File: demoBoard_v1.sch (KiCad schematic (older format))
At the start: 55 parts, among them P1 SPI_Header, P10 RTC_Serial, P11 WD_Header, P12 WD_1.2V_NC, P13 RTC_Aux, P14 Flash_3v3_NC, P15 WD_SENSE_3.3V_NC, P2 3x_CS_Header, P3 Power_Header, P4 LOAD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

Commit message: Updated footprints for headers in schematic
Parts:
- P1, P13, P2, P6, P7: footprint SFUSat:3x_01In_Header -> SFUSat:3x_01In_Header_v2
- P10: footprint SFUSat:4x01In_Header -> SFUSat:4x01In_Header_v2
- P11, P12, P14, P15, P3, P4, P5, P8, P9: footprint SFUSat:2x01In_Header -> SFUSat:2x01In_Header_v2
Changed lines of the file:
@@
 F 0 "P1" H 1750 2600 50  0000 C CNN
 F 1 "SPI_Header" V 1850 2400 50  0000 C CNN
-F 2 "SFUSat:3x_01In_Header" H 1750 2400 50  0001 C CNN
+F 2 "SFUSat:3x_01In_Header_v2" H 1750 2400 50  0001 C CNN
 F 3 "" H 1750 2400 50  0000 C CNN
 	1    1750 2400
@@
 F 0 "P2" H 2950 2650 50  0000 C CNN
 F 1 "3x_CS_Header" V 3050 2450 50  0000 C CNN
-F 2 "SFUSat:3x_01In_Header" H 2950 2450 50  0001 C CNN
+F 2 "SFUSat:3x_01In_Header_v2" H 2950 2450 50  0001 C CNN
 F 3 "" H 2950 2450 50  0000 C CNN
 	1    2950 2450
@@
 F 0 "P3" H 5000 6900 50  0000 C CNN
 F 1 "Power_Header" V 5100 6750 50  0000 C CNN
-F 2 "SFUSat:2x01In_Header" H 5000 6750 50  0001 C CNN
+F 2 "SFUSat:2x01In_Header_v2" H 5000 6750 50  0001 C CNN
 F 3 "" H 5000 6750 50  0000 C CNN
 	1    5000 6750
@@
 F 0 "P10" H 8100 6400 50  0000 C CNN
 F 1 "RTC_Serial" V 8200 6150 50  0000 C CNN
-F 2 "SFUSat:4x01In_Header" H 8100 6150 50  0001 C CNN
+F 2 "SFUSat:4x01In_Header_v2" H 8100 6150 50  0001 C CNN
 F 3 "" H 8100 6150 50  0000 C CNN
 	1    8100 6150
@@
 F 0 "P13" H 10050 6350 50  0000 C CNN
 F 1 "RTC_Aux" V 10150 6150 50  0000 C CNN
-F 2 "SFUSat:3x_01In_Header" H 10050 6150 50  0001 C CNN
+F 2 "SFUSat:3x_01In_Header_v2" H 10050 6150 50  0001 C CNN
 F 3 "" H 10050 6150 50  0000 C CNN
 	1    10050 6150
@@
 F 0 "P7" H 3950 4150 50  0000 C CNN
 F 1 "INA_Power" V 4050 3950 50  0000 C CNN
-F 2 "SFUSat:3x_01In_Header" H 3950 3950 50  0001 C CNN
+F 2 "SFUSat:3x_01In_Header_v2" H 3950 3950 50  0001 C CNN
 F 3 "" H 3950 3950 50  0000 C CNN
 	1    3950 3950
@@
 F 0 "P6" H 2350 3400 50  0000 C CNN
 F 1 "INA_GND" V 2450 3200 50  0000 C CNN
-F 2 "SFUSat:3x_01In_Header" H 2350 3200 50  0001 C CNN
+F 2 "SFUSat:3x_01In_Header_v2" H 2350 3200 50  0001 C CNN
 F 3 "" H 2350 3200 50  0000 C CNN
 	1    2350 3200
@@
 F 0 "P5" H 1650 3350 50  0000 C CNN
 F 1 "INA_Signal" V 1750 3200 50  0000 C CNN
-F 2 "SFUSat:2x01In_Header" H 1650 3200 50  0001 C CNN
+F 2 "SFUSat:2x01In_Header_v2" H 1650 3200 50  0001 C CNN
 F 3 "" H 1650 3200 50  0000 C CNN
 	1    1650 3200
@@
 F 0 "P11" H 9650 3900 50  0000 C CNN
 F 1 "WD_Header" V 9750 3750 50  0000 C CNN
-F 2 "SFUSat:2x01In_Header" H 9650 3750 50  0001 C CNN
+F 2 "SFUSat:2x01In_Header_v2" H 9650 3750 50  0001 C CNN
 F 3 "" H 9650 3750 50  0000 C CNN
 	1    9650 3750
@@
 F 0 "P4" H 1000 3350 50  0000 C CNN
 F 1 "LOAD" V 1100 3200 50  0000 C CNN
-F 2 "SFUSat:2x01In_Header" H 1000 3200 50  0001 C CNN
+F 2 "SFUSat:2x01In_Header_v2" H 1000 3200 50  0001 C CNN
 F 3 "" H 1000 3200 50  0000 C CNN
 	1    1000 3200
@@
 F 0 "P14" H 10450 1200 50  0000 C CNN
 F 1 "Flash_3v3_NC" V 10550 1050 50  0000 C CNN
-F 2 "SFUSat:2x01In_Header" H 10450 1050 50  0001 C CNN
+F 2 "SFUSat:2x01In_Header_v2" H 10450 1050 50  0001 C CNN
 F 3 "" H 10450 1050 50  0000 C CNN
 	1    10450 1050
@@
 F 0 "P8" H 6000 2450 50  0000 C CNN
 F 1 "1.2V_3.3V_NC" V 6100 2300 50  0000 C CNN
-F 2 "SFUSat:2x01In_Header" H 6000 2300 50  0001 C CNN
+F 2 "SFUSat:2x01In_Header_v2" H 6000 2300 50  0001 C CNN
 F 3 "" H 6000 2300 50  0000 C CNN
 	1    6000 2300
@@
 F 0 "P12" H 10050 2500 50  0000 C CNN
 F 1 "WD_1.2V_NC" V 10150 2350 50  0000 C CNN
-F 2 "SFUSat:2x01In_Header" H 10050 2350 50  0001 C CNN
+F 2 "SFUSat:2x01In_Header_v2" H 10050 2350 50  0001 C CNN
 F 3 "" H 10050 2350 50  0000 C CNN
 	1    10050 2350
@@
 F 0 "P9" H 7950 4550 50  0000 C CNN
 F 1 "RTC_3.3_NC" V 8050 4400 50  0000 C CNN
-F 2 "SFUSat:2x01In_Header" H 7950 4400 50  0001 C CNN
+F 2 "SFUSat:2x01In_Header_v2" H 7950 4400 50  0001 C CNN
 F 3 "" H 7950 4400 50  0000 C CNN
 	1    7950 4400
@@
 F 0 "P15" H 10650 2650 50  0000 C CNN
 F 1 "WD_SENSE_3.3V_NC" V 10750 2500 50  0000 C CNN
-F 2 "SFUSat:2x01In_Header" H 10650 2500 50  0001 C CNN
+F 2 "SFUSat:2x01In_Header_v2" H 10650 2500 50  0001 C CNN
 F 3 "" H 10650 2500 50  0000 C CNN
 	1    10650 2500

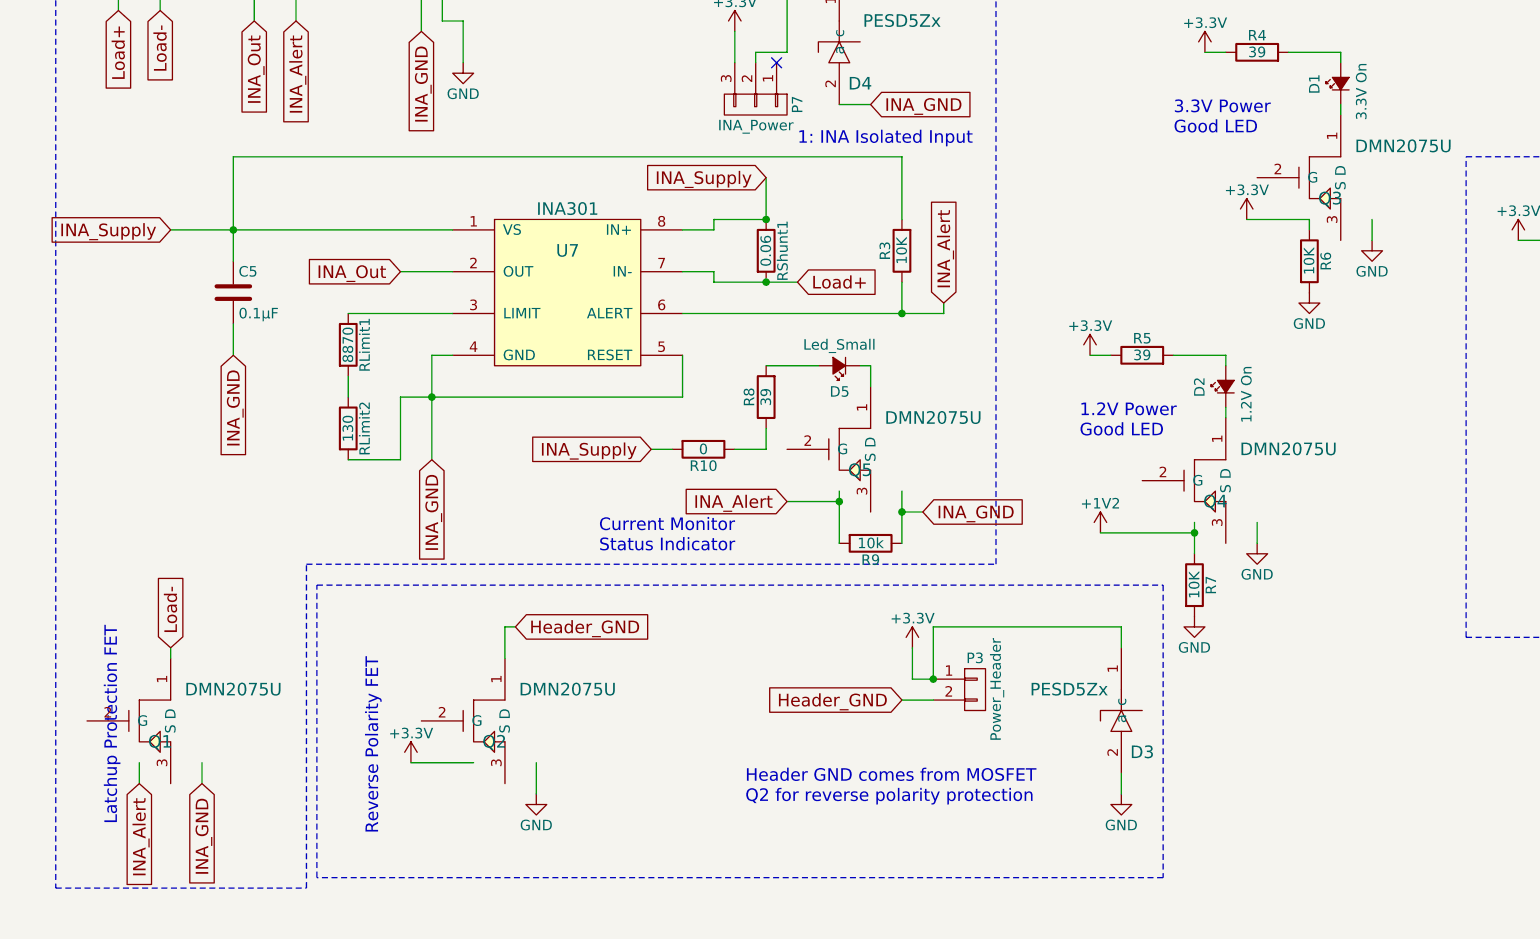
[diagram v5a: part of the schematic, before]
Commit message: Updated DMN2075 MOSFET symbol
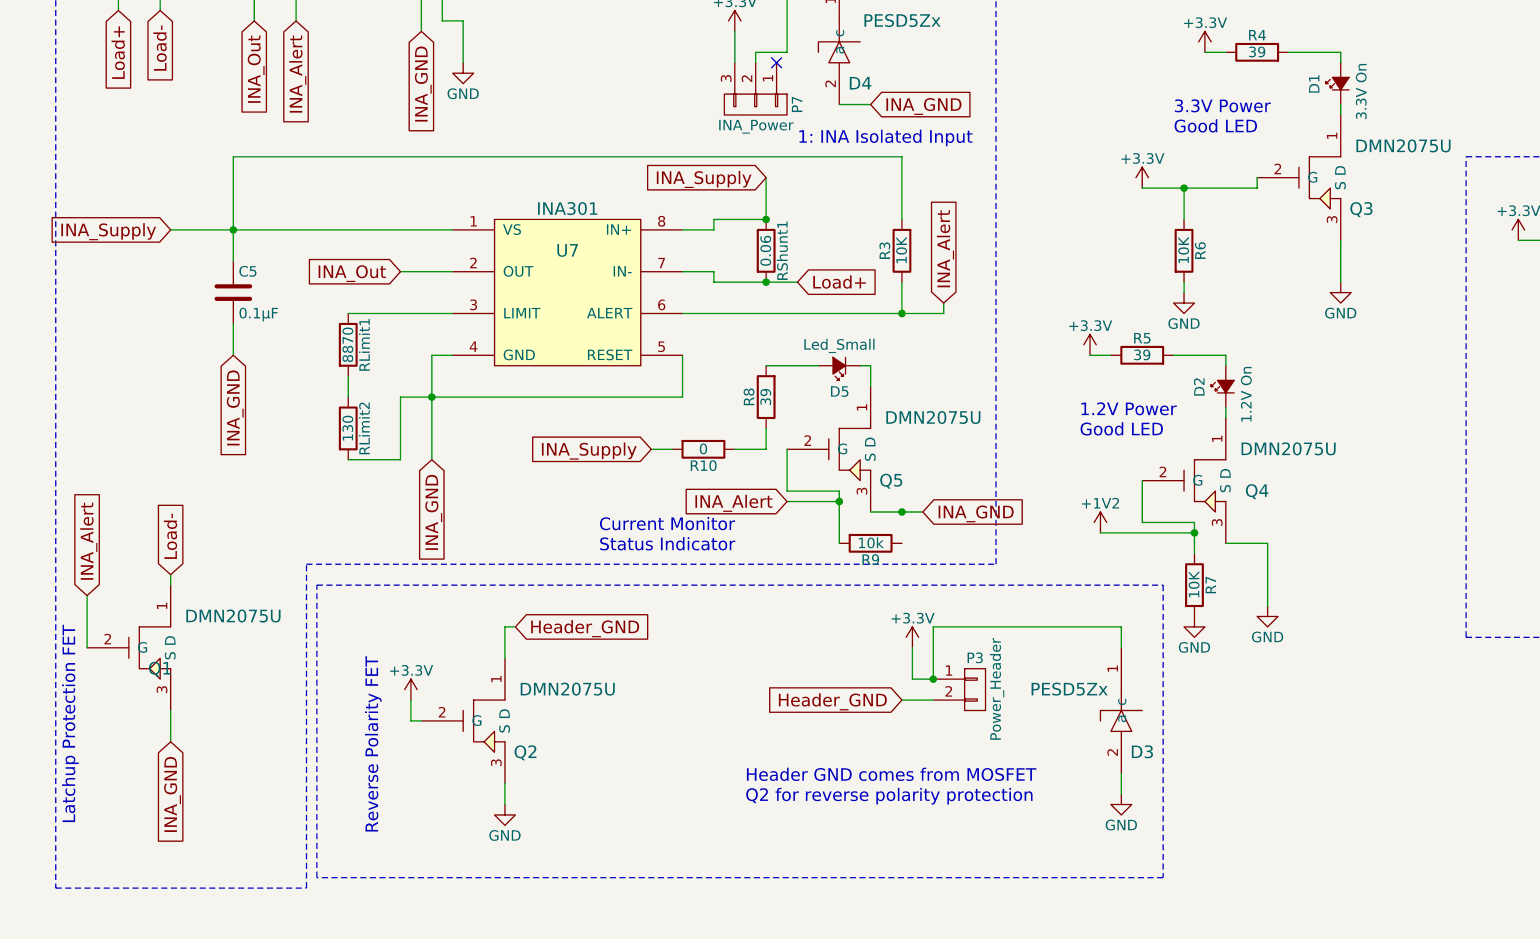
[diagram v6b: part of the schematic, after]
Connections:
- wire segments 187 -> 194
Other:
- moved on the sheet: Q1, R6
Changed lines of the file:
@@
 L DMN2075U Q1
 U 1 1 592245CD
-P 1150 6900
-F 0 "Q1" H 1100 6800 60  0000 C CNN
-F 1 "DMN2075U" H 1450 7050 60  0000 C CNN
-F 2 "SFUSat:SOT23_DMN2075U" H 1100 6800 60  0001 C CNN
-F 3 "" H 1100 6800 60  0001 C CNN
-	1    1150 6900
-	1    0    0    -1
-$EndComp
-Text GLabel 1000 7200 3    60   Input ~ 0
+P 1150 6550
+F 0 "Q1" H 1100 6450 60  0000 C CNN
+F 1 "DMN2075U" H 1450 6700 60  0000 C CNN
+F 2 "SFUSat:SOT23_DMN2075U" H 1100 6450 60  0001 C CNN
+F 3 "" H 1100 6450 60  0001 C CNN
+	1    1150 6550
+	1    0    0    -1
+$EndComp
+Text GLabel 750  6300 1    60   Input ~ 0
 INA_Alert
-Text GLabel 1150 6550 1    60   Input ~ 0
+Text GLabel 1150 6200 1    60   Input ~ 0
 Load-
-Text GLabel 1300 7200 3    60   Input ~ 0
+Text GLabel 1150 7000 3    60   Input ~ 0
 INA_GND
-Text Notes 900  6450 3    60   ~ 0
+Text Notes 700  6450 3    60   ~ 0
 Latchup Protection FET\n
 $Comp
@@
 U 1 1 592259E3
 P 2750 6900
-F 0 "Q2" H 2700 6800 60  0000 C CNN
+F 0 "Q2" H 2850 6750 60  0000 C CNN
 F 1 "DMN2075U" H 3050 7050 60  0000 C CNN
 F 2 "SFUSat:SOT23_DMN2075U" H 2700 6800 60  0001 C CNN
@@
 L +3.3V #PWR024
 U 1 1 59225ADF
-P 2300 7100
-F 0 "#PWR024" H 2300 6950 50  0001 C CNN
-F 1 "+3.3V" H 2300 7240 50  0000 C CNN
-F 2 "" H 2300 7100 50  0000 C CNN
-F 3 "" H 2300 7100 50  0000 C CNN
-	1    2300 7100
+P 2300 6800
+F 0 "#PWR024" H 2300 6650 50  0001 C CNN
+F 1 "+3.3V" H 2300 6940 50  0000 C CNN
+F 2 "" H 2300 6800 50  0000 C CNN
+F 3 "" H 2300 6800 50  0000 C CNN
+	1    2300 6800
 	1    0    0    -1
 $EndComp
@@
 L GND #PWR025
 U 1 1 59225BBB
-P 2900 7250
-F 0 "#PWR025" H 2900 7000 50  0001 C CNN
-F 1 "GND" H 2900 7100 50  0000 C CNN
-F 2 "" H 2900 7250 50  0000 C CNN
-F 3 "" H 2900 7250 50  0000 C CNN
-	1    2900 7250
+P 2750 7300
+F 0 "#PWR025" H 2750 7050 50  0001 C CNN
+F 1 "GND" H 2750 7150 50  0000 C CNN
+F 2 "" H 2750 7300 50  0000 C CNN
+F 3 "" H 2750 7300 50  0000 C CNN
+	1    2750 7300
 	1    0    0    -1
 $EndComp
@@
 U 1 1 5922725B
 P 6750 4300
-F 0 "Q3" H 6700 4200 60  0000 C CNN
+F 0 "Q3" H 6850 4150 60  0000 C CNN
 F 1 "DMN2075U" H 7050 4450 60  0000 C CNN
 F 2 "SFUSat:SOT23_DMN2075U" H 6700 4200 60  0001 C CNN
@@
 U 1 1 59227491
 P 6200 5750
-F 0 "Q4" H 6150 5650 60  0000 C CNN
+F 0 "Q4" H 6350 5700 60  0000 C CNN
 F 1 "DMN2075U" H 6500 5900 60  0000 C CNN
 F 2 "SFUSat:SOT23_DMN2075U" H 6150 5650 60  0001 C CNN
@@
 L GND #PWR026
 U 1 1 5922769E
-P 6900 4600
-F 0 "#PWR026" H 6900 4350 50  0001 C CNN
-F 1 "GND" H 6900 4450 50  0000 C CNN
-F 2 "" H 6900 4600 50  0000 C CNN
-F 3 "" H 6900 4600 50  0000 C CNN
-	1    6900 4600
+P 6750 4800
+F 0 "#PWR026" H 6750 4550 50  0001 C CNN
+F 1 "GND" H 6750 4650 50  0000 C CNN
+F 2 "" H 6750 4800 50  0000 C CNN
+F 3 "" H 6750 4800 50  0000 C CNN
+	1    6750 4800
 	1    0    0    -1
 $EndComp
@@
 L GND #PWR029
 U 1 1 5922784B
-P 6350 6050
-F 0 "#PWR029" H 6350 5800 50  0001 C CNN
-F 1 "GND" H 6350 5900 50  0000 C CNN
-F 2 "" H 6350 6050 50  0000 C CNN
-F 3 "" H 6350 6050 50  0000 C CNN
-	1    6350 6050
+P 6400 6350
+F 0 "#PWR029" H 6400 6100 50  0001 C CNN
+F 1 "GND" H 6400 6200 50  0000 C CNN
+F 2 "" H 6400 6350 50  0000 C CNN
+F 3 "" H 6400 6350 50  0000 C CNN
+	1    6400 6350
 	1    0    0    -1
 $EndComp
@@
 L +3.3V #PWR031
 U 1 1 59227969
-P 6300 4500
-F 0 "#PWR031" H 6300 4350 50  0001 C CNN
-F 1 "+3.3V" H 6300 4640 50  0000 C CNN
-F 2 "" H 6300 4500 50  0000 C CNN
-F 3 "" H 6300 4500 50  0000 C CNN
-	1    6300 4500
+P 5800 4350
+F 0 "#PWR031" H 5800 4200 50  0001 C CNN
+F 1 "+3.3V" H 5800 4490 50  0000 C CNN
+F 2 "" H 5800 4350 50  0000 C CNN
+F 3 "" H 5800 4350 50  0000 C CNN
+	1    5800 4350
 	1    0    0    -1
 $EndComp
@@
 L R R6
 U 1 1 59229722
-P 6600 4700
-F 0 "R6" V 6680 4700 50  0000 C CNN
-F 1 "10K" V 6600 4700 50  0000 C CNN
-F 2 "Resistors_SMD:R_0402" V 6530 4700 50  0001 C CNN
-F 3 "" H 6600 4700 50  0000 C CNN
-	1    6600 4700
+P 6000 4650
+F 0 "R6" V 6080 4650 50  0000 C CNN
+F 1 "10K" V 6000 4650 50  0000 C CNN
+F 2 "Resistors_SMD:R_0402" V 5930 4650 50  0001 C CNN
+F 3 "" H 6000 4650 50  0000 C CNN
+	1    6000 4650
 	1    0    0    -1
 $EndComp
@@
 L GND #PWR033
 U 1 1 59229C2B
-P 6600 4850
-F 0 "#PWR033" H 6600 4600 50  0001 C CNN
-F 1 "GND" H 6600 4700 50  0000 C CNN
-F 2 "" H 6600 4850 50  0000 C CNN
-F 3 "" H 6600 4850 50  0000 C CNN
-	1    6600 4850
+P 6000 4850
+F 0 "#PWR033" H 6000 4600 50  0001 C CNN
+F 1 "GND" H 6000 4700 50  0000 C CNN
+F 2 "" H 6000 4850 50  0000 C CNN
+F 3 "" H 6000 4850 50  0000 C CNN
+	1    6000 4850
 	1    0    0    -1
 $EndComp
@@
 U 1 1 592523F8
 P 4500 5600
-F 0 "Q5" H 4450 5500 60  0000 C CNN
+F 0 "Q5" H 4600 5450 60  0000 C CNN
 F 1 "DMN2075U" H 4800 5750 60  0000 C CNN
 F 2 "SFUSat:SOT23_DMN2075U" H 4450 5500 60  0001 C CNN
@@
 	950  3400 900  3400
 Wire Wire Line
-	1000 7100 1000 7200
-Wire Wire Line
-	1300 7100 1300 7200
-Wire Wire Line
-	1150 6600 1150 6550
+	1150 6250 1150 6200
 Wire Wire Line
 	2800 6450 2750 6450
 Wire Wire Line
 	2750 6450 2750 6600
-Wire Wire Line
-	2600 7100 2300 7100
-Wire Wire Line
-	2900 7100 2900 7250
 Wire Notes Line
 	600  7700 1800 7700
@@
 	6750 3950 6750 4000
 Wire Wire Line
-	6600 4500 6300 4500
-Wire Wire Line
-	6900 4500 6900 4600
+	6750 4600 6750 4800
 Wire Wire Line
 	5650 5150 5550 5150
@@
 	5600 6000 6050 6000
 Wire Wire Line
-	6350 5950 6350 6050
-Wire Wire Line
-	6600 4550 6600 4500
+	6400 6050 6400 6350
 Wire Wire Line
 	6050 5950 6050 6100
@@
 INA_GND
 Wire Wire Line
-	4650 5800 4650 6050
-Wire Wire Line
-	4650 5900 4750 5900
+	4500 5900 4750 5900
 Text GLabel 4100 5850 0    60   Input ~ 0
 INA_Alert
@@
 Wire Wire Line
 	2250 5650 2250 5350
+Wire Wire Line
+	5800 4350 6350 4350
+Wire Wire Line
+	6000 4350 6000 4500
+Wire Wire Line
+	6000 4800 6000 4850
+Wire Wire Line
+	6350 4350 6350 4300
+Connection ~ 6000 4350
+Wire Wire Line
+	5800 5750 5800 5950
+Wire Wire Line
+	5800 5950 6050 5950
+Wire Wire Line
+	6200 6050 6400 6050
+Wire Wire Line
+	2300 6800 2300 6900
+Wire Wire Line
+	2300 6900 2350 6900
+Wire Wire Line
+	2750 7200 2750 7300
+Wire Wire Line
+	750  6300 750  6550
+Wire Wire Line
+	1150 6850 1150 7000
+Wire Wire Line
+	4100 5600 4100 5800
+Wire Wire Line
+	4100 5800 4350 5800
 $EndSCHEMATC

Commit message: Updated 0402 capacitor in library. Haven't updated footprints on PCB, although they could be changed.
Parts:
- C1, C2, C3, C5, C6, C7, C8, C9: footprint Capacitors_SMD:C_0402 -> SFUSat:C_0402
- R1, R10, R2, R3, R4, R5, R6, R7, R8, R9, RLimit1, RLimit2: footprint Resistors_SMD:R_0402 -> SFUSat:R_0402
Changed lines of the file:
@@
 F 0 "C1" H 5825 2900 50  0000 L CNN
 F 1 "1µF" H 5825 2700 50  0000 L CNN
-F 2 "Capacitors_SMD:C_0402" H 5838 2650 50  0001 C CNN
+F 2 "SFUSat:C_0402" H 5838 2650 50  0001 C CNN
 F 3 "" H 5800 2800 50  0000 C CNN
 	1    5800 2800
@@
 F 0 "C2" H 7575 3000 50  0000 L CNN
 F 1 "1µF" H 7575 2800 50  0000 L CNN
-F 2 "Capacitors_SMD:C_0402" H 7588 2750 50  0001 C CNN
+F 2 "SFUSat:C_0402" H 7588 2750 50  0001 C CNN
 F 3 "" H 7550 2900 50  0000 C CNN
 	1    7550 2900
@@
 F 0 "R1" V 10930 3000 50  0000 C CNN
 F 1 "820K" V 10850 3000 50  0000 C CNN
-F 2 "Resistors_SMD:R_0402" V 10780 3000 50  0001 C CNN
+F 2 "SFUSat:R_0402" V 10780 3000 50  0001 C CNN
 F 3 "" H 10850 3000 50  0000 C CNN
 	1    10850 3000
@@
 F 0 "R2" V 10930 3500 50  0000 C CNN
 F 1 "180K" V 10850 3500 50  0000 C CNN
-F 2 "Resistors_SMD:R_0402" V 10780 3500 50  0001 C CNN
+F 2 "SFUSat:R_0402" V 10780 3500 50  0001 C CNN
 F 3 "" H 10850 3500 50  0000 C CNN
 	1    10850 3500
@@
 F 0 "C3" H 8025 5000 50  0000 L CNN
 F 1 "10nF" H 8025 4800 50  0000 L CNN
-F 2 "Capacitors_SMD:C_0402" H 8038 4750 50  0001 C CNN
+F 2 "SFUSat:C_0402" H 8038 4750 50  0001 C CNN
 F 3 "" H 8000 4900 50  0000 C CNN
 	1    8000 4900
@@
 F 0 "R3" V 4730 4650 50  0000 C CNN
 F 1 "10K" V 4650 4650 50  0000 C CNN
-F 2 "Resistors_SMD:R_0402" V 4580 4650 50  0001 C CNN
+F 2 "SFUSat:R_0402" V 4580 4650 50  0001 C CNN
 F 3 "" H 4650 4650 50  0000 C CNN
 	1    4650 4650
@@
 F 0 "C5" H 1475 4950 50  0000 L CNN
 F 1 "0.1µF" H 1475 4750 50  0000 L CNN
-F 2 "Capacitors_SMD:C_0402" H 1488 4700 50  0001 C CNN
+F 2 "SFUSat:C_0402" H 1488 4700 50  0001 C CNN
 F 3 "" H 1450 4850 50  0000 C CNN
 	1    1450 4850
@@
 F 0 "RLimit1" V 2080 5100 50  0000 C CNN
 F 1 "8870" V 2000 5100 50  0000 C CNN
-F 2 "Resistors_SMD:R_0402" V 1930 5100 50  0001 C CNN
+F 2 "SFUSat:R_0402" V 1930 5100 50  0001 C CNN
 F 3 "" H 2000 5100 50  0000 C CNN
 	1    2000 5100
@@
 F 0 "C8" H 9575 1200 50  0000 L CNN
 F 1 "0.1µF" H 9575 1000 50  0000 L CNN
-F 2 "Capacitors_SMD:C_0402" H 9588 950 50  0001 C CNN
+F 2 "SFUSat:C_0402" H 9588 950 50  0001 C CNN
 F 3 "" H 9550 1100 50  0000 C CNN
 	1    9550 1100
@@
 F 0 "C7" H 6525 1200 50  0000 L CNN
 F 1 "0.1µF" H 6525 1000 50  0000 L CNN
-F 2 "Capacitors_SMD:C_0402" H 6538 950 50  0001 C CNN
+F 2 "SFUSat:C_0402" H 6538 950 50  0001 C CNN
 F 3 "" H 6500 1100 50  0000 C CNN
 	1    6500 1100
@@
 F 0 "C6" H 3525 1200 50  0000 L CNN
 F 1 "0.1µF" H 3525 1000 50  0000 L CNN
-F 2 "Capacitors_SMD:C_0402" H 3538 950 50  0001 C CNN
+F 2 "SFUSat:C_0402" H 3538 950 50  0001 C CNN
 F 3 "" H 3500 1100 50  0000 C CNN
 	1    3500 1100
@@
 F 0 "C9" H 10375 2900 50  0000 L CNN
 F 1 "0.1µF" H 10375 2700 50  0000 L CNN
-F 2 "Capacitors_SMD:C_0402" H 10388 2650 50  0001 C CNN
+F 2 "SFUSat:C_0402" H 10388 2650 50  0001 C CNN
 F 3 "" H 10350 2800 50  0000 C CNN
 	1    10350 2800
@@
 F 0 "R4" V 6430 3700 50  0000 C CNN
 F 1 "39" V 6350 3700 50  0000 C CNN
-F 2 "Resistors_SMD:R_0402" V 6280 3700 50  0001 C CNN
+F 2 "SFUSat:R_0402" V 6280 3700 50  0001 C CNN
 F 3 "" H 6350 3700 50  0000 C CNN
 	1    6350 3700
@@
 F 0 "R5" V 5880 5150 50  0000 C CNN
 F 1 "39" V 5800 5150 50  0000 C CNN
-F 2 "Resistors_SMD:R_0402" V 5730 5150 50  0001 C CNN
+F 2 "SFUSat:R_0402" V 5730 5150 50  0001 C CNN
 F 3 "" H 5800 5150 50  0000 C CNN
 	1    5800 5150
@@
 F 0 "R6" V 6080 4650 50  0000 C CNN
 F 1 "10K" V 6000 4650 50  0000 C CNN
-F 2 "Resistors_SMD:R_0402" V 5930 4650 50  0001 C CNN
+F 2 "SFUSat:R_0402" V 5930 4650 50  0001 C CNN
 F 3 "" H 6000 4650 50  0000 C CNN
 	1    6000 4650
@@
 F 0 "R7" V 6130 6250 50  0000 C CNN
 F 1 "10K" V 6050 6250 50  0000 C CNN
-F 2 "Resistors_SMD:R_0402" V 5980 6250 50  0001 C CNN
+F 2 "SFUSat:R_0402" V 5980 6250 50  0001 C CNN
 F 3 "" H 6050 6250 50  0000 C CNN
 	1    6050 6250
@@
 F 0 "R8" V 4080 5350 50  0000 C CNN
 F 1 "39" V 4000 5350 50  0000 C CNN
-F 2 "Resistors_SMD:R_0402" V 3930 5350 50  0001 C CNN
+F 2 "SFUSat:R_0402" V 3930 5350 50  0001 C CNN
 F 3 "" H 4000 5350 50  0000 C CNN
 	1    4000 5350
@@
 F 0 "R9" V 4580 6050 50  0000 C CNN
 F 1 "10k" V 4500 6050 50  0000 C CNN
-F 2 "Resistors_SMD:R_0402" V 4430 6050 50  0001 C CNN
+F 2 "SFUSat:R_0402" V 4430 6050 50  0001 C CNN
 F 3 "" H 4500 6050 50  0000 C CNN
 	1    4500 6050
@@
 F 0 "R10" V 3780 5600 50  0000 C CNN
 F 1 "0" V 3700 5600 50  0000 C CNN
-F 2 "Resistors_SMD:R_0402" V 3630 5600 50  0001 C CNN
+F 2 "SFUSat:R_0402" V 3630 5600 50  0001 C CNN
 F 3 "" H 3700 5600 50  0000 C CNN
 	1    3700 5600
@@
 F 0 "RLimit2" V 2080 5500 50  0000 C CNN
 F 1 "130" V 2000 5500 50  0000 C CNN
-F 2 "Resistors_SMD:R_0402" V 1930 5500 50  0001 C CNN
+F 2 "SFUSat:R_0402" V 1930 5500 50  0001 C CNN
 F 3 "" H 2000 5500 50  0000 C CNN
 	1    2000 5500
